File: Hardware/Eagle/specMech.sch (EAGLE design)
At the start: 88 parts, among them J1 PINHD-1X8-MOLEX-SHROUD, J2 MOLEX-22112022, J3 PINHD-1X8-MOLEX-SHROUD, J4 PINHD-1X8-MOLEX-SHROUD, J6 Molex 0022232081, J7 Lantronix XPORT, J8 Molex 0022232081, U1 MCP23008-E/SO, U10 ADS1115, U11 MCP23008-E/SO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

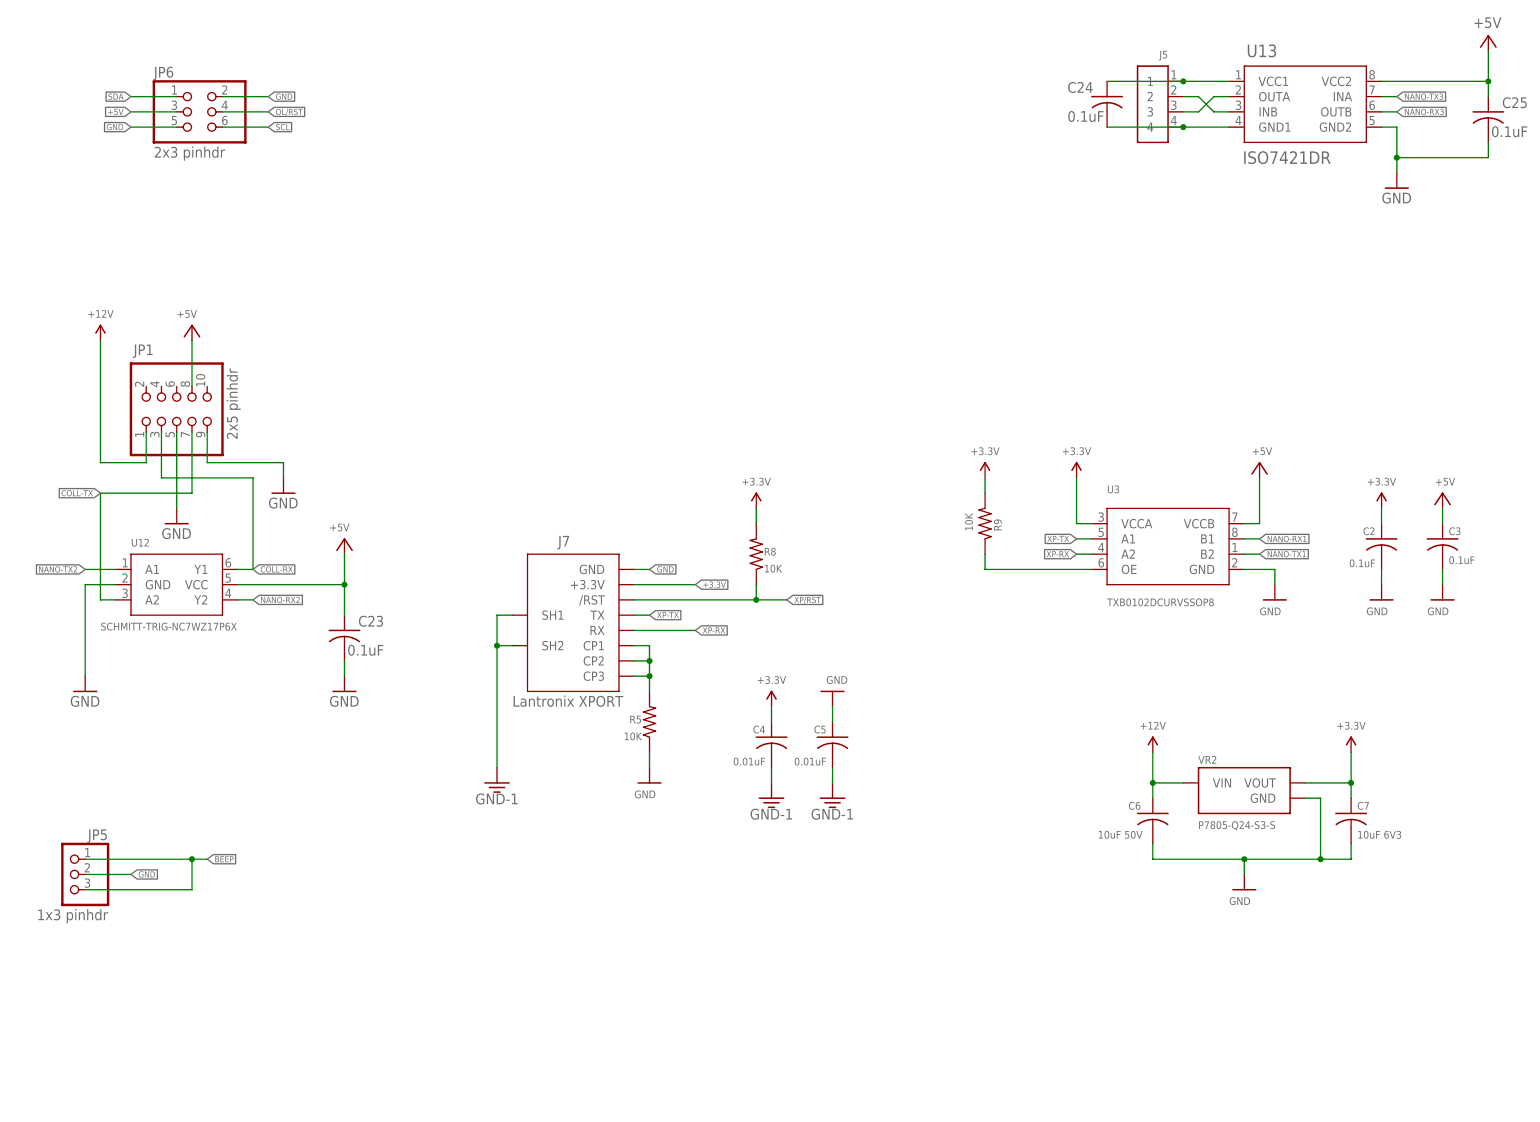
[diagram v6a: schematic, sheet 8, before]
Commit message: Added fan control
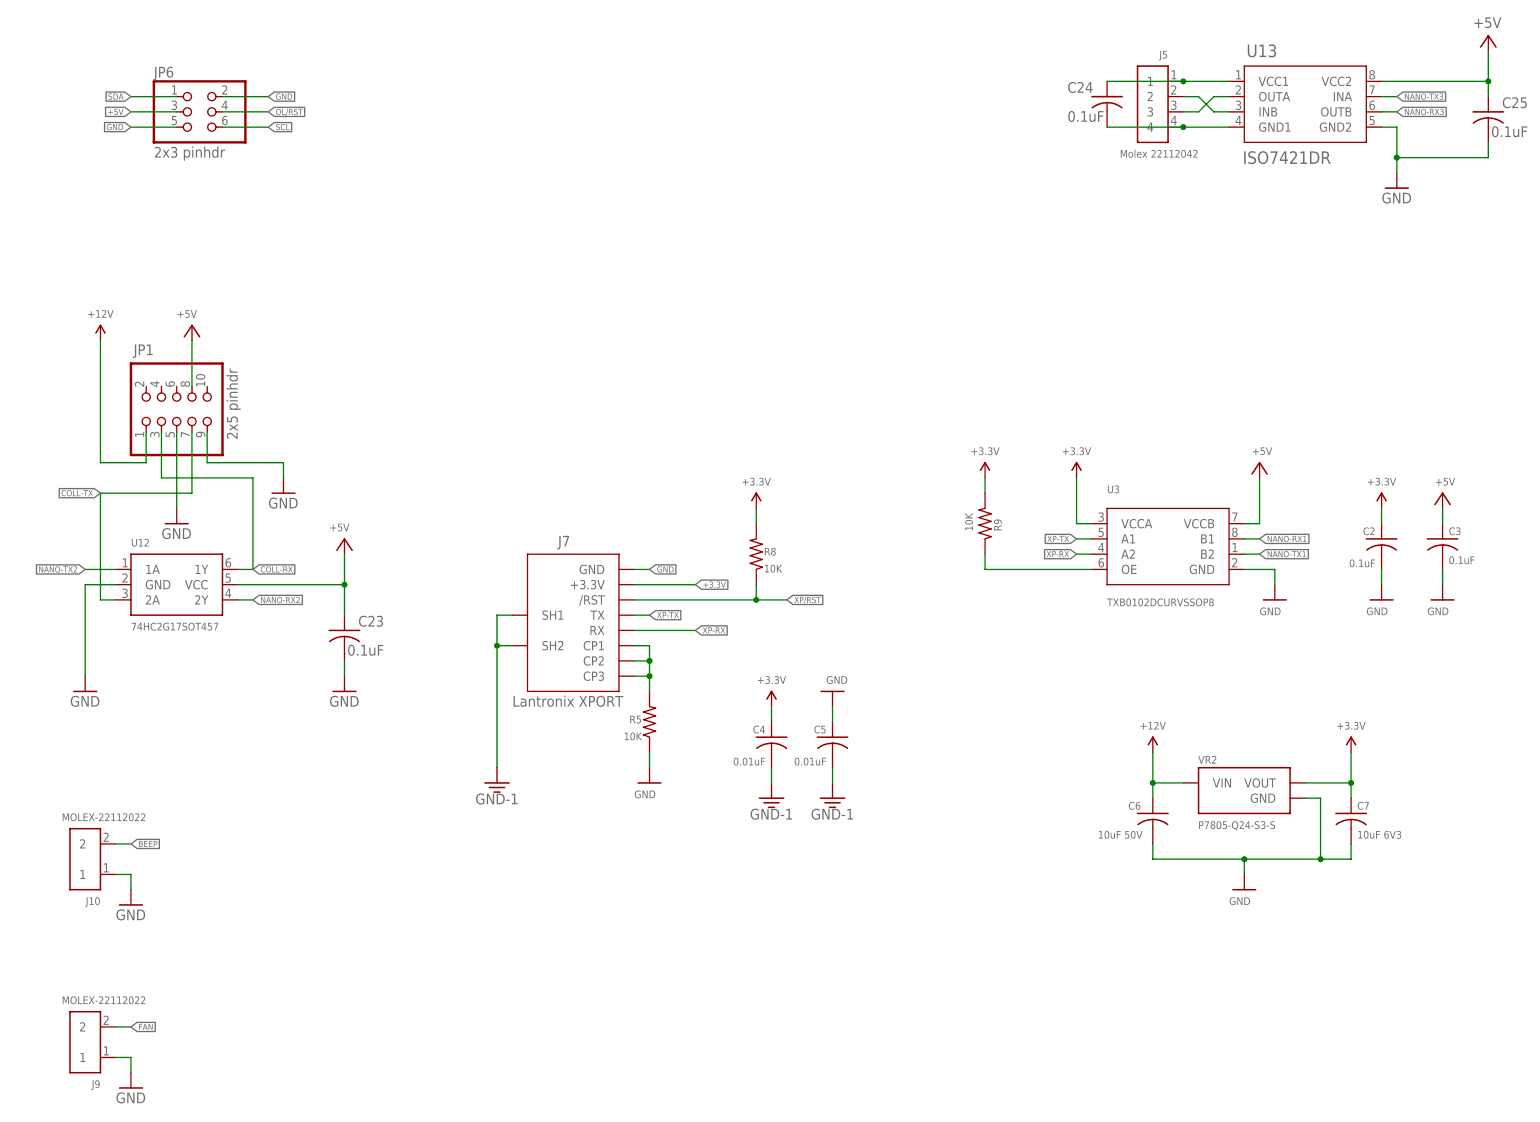
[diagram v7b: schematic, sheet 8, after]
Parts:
- removed JP5: 1x3 pinhdr, AUmlib:PINHD-1X3
- added J10, J9: MOLEX-22112022, AUmlib:PINHD-1X2-MOLEX-22112022
- J5: value (none) -> Molex 22112042
- U12: value SCHMITT-TRIG-NC7WZ17P6X -> 74HC2G17SOT457; device AUmlib:SCHMITT-TRIG-NC7WZ17P6X -> AUmlib:74HC2G17SOT457
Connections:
- new net FAN: CNANO1.PB3, J9.2
- net BEEP: now also J10.2; no longer JP5.1, JP5.3
- net COLL-RX: now also U12.1Y; no longer U12.Y1
- net COLL-TX: now also U12.2A; no longer U12.A2
- net GND: now also J10.1, J9.1; no longer JP5.2
- net NANO-RX2: now also U12.2Y; no longer U12.Y2
- net NANO-TX2: now also U12.1A; no longer U12.A1
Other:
- note added: "Fan"
- note removed: "Change to 2-pin polarized header"
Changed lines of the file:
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@@
 <setting verticaltext="up"/>
 </settings>
-<grid distance="0.1" unitdist="inch" unit="inch" style="lines" multiple="1" display="yes" altdistance="0.01" altunitdist="inch" altunit="inch"/>
+<grid distance="0.1" unitdist="inch" unit="inch" style="lines" multiple="1" display="no" altdistance="0.01" altunitdist="inch" altunit="inch"/>
 <layers>
 <layer number="1" name="Top" color="4" fill="1" visible="no" active="no"/>
@@
 <part name="JP6" library="AUmlib" library_urn="urn:adsk.eagle:library:9166017" deviceset="PINHD-2X3" device="" package3d_urn="urn:adsk.eagle:package:24493429/1" value="2x3 pinhdr"/>
 <part name="JP1" library="AUmlib" library_urn="urn:adsk.eagle:library:9166017" deviceset="PINHD-2X5" device="" package3d_urn="urn:adsk.eagle:package:24435877/1" value="2x5 pinhdr"/>
-<part name="U12" library="AUmlib" library_urn="urn:adsk.eagle:library:9166017" deviceset="SCHMITT-TRIG-NC7WZ17P6X" device="" package3d_urn="urn:adsk.eagle:package:26421290/2"/>
+<part name="U12" library="AUmlib" library_urn="urn:adsk.eagle:library:9166017" deviceset="74HC2G17" device="SOT457" package3d_urn="urn:adsk.eagle:package:9152015/2"/>
 <part name="GND28" library="AUmlib" library_urn="urn:adsk.eagle:library:9166017" deviceset="GND" device=""/>
 <part name="P+12" library="AUmlib" library_urn="urn:adsk.eagle:library:9166017" deviceset="+5V" device=""/>
@@
 <part name="GND41" library="AUmlib" library_urn="urn:adsk.eagle:library:9166017" deviceset="GND" device=""/>
 <part name="GND42" library="AUmlib" library_urn="urn:adsk.eagle:library:9166017" deviceset="GND" device=""/>
-<part name="JP5" library="AUmlib" library_urn="urn:adsk.eagle:library:9166017" deviceset="PINHD-1X3" device="" package3d_urn="urn:adsk.eagle:package:21589412/1" value="1x3 pinhdr"/>
 <part name="U7" library="AUmlib" library_urn="urn:adsk.eagle:library:9166017" deviceset="LTC4311ISC6TRPBF" device="" package3d_urn="urn:adsk.eagle:package:24435366/2"/>
 <part name="C22" library="AUmlib" library_urn="urn:adsk.eagle:library:9166017" deviceset="C-US" device="C0805" package3d_urn="urn:adsk.eagle:package:4021265/3" value="0.1uF"/>
@@
 <part name="TVS1" library="AUmlib" library_urn="urn:adsk.eagle:library:9166017" deviceset="TVS-QUAD-ESDA6V1BC6" device="" package3d_urn="urn:adsk.eagle:package:25920714/2"/>
 <part name="TVS2" library="AUmlib" library_urn="urn:adsk.eagle:library:9166017" deviceset="TVS-QUAD-ESDA6V1BC6" device="" package3d_urn="urn:adsk.eagle:package:25920714/2"/>
-<part name="J5" library="AUmlib" library_urn="urn:adsk.eagle:library:9166017" deviceset="PINHD-1X4-MOLEX-22112042" device="" package3d_urn="urn:adsk.eagle:package:24729143/2"/>
+<part name="J5" library="AUmlib" library_urn="urn:adsk.eagle:library:9166017" deviceset="PINHD-1X4-MOLEX-22112042" device="" package3d_urn="urn:adsk.eagle:package:24729143/2" value="Molex 22112042"/>
+<part name="J9" library="AUmlib" library_urn="urn:adsk.eagle:library:9166017" deviceset="PINHD-1X2-MOLEX-22112022" device="" package3d_urn="urn:adsk.eagle:package:24727026/5" value="MOLEX-22112022"/>
+<part name="GND46" library="AUmlib" library_urn="urn:adsk.eagle:library:9166017" deviceset="GND" device=""/>
+<part name="J10" library="AUmlib" library_urn="urn:adsk.eagle:library:9166017" deviceset="PINHD-1X2-MOLEX-22112022" device="" package3d_urn="urn:adsk.eagle:package:24727026/5" value="MOLEX-22112022"/>
+<part name="GND47" library="AUmlib" library_urn="urn:adsk.eagle:library:9166017" deviceset="GND" device=""/>
 </parts>
 <sheets>
@@
 </segment>
 </net>
+<net name="FAN" class="0">
+<segment>
+<pinref part="CNANO1" gate="G$1" pin="PB3"/>
+<wire x1="88.9" y1="91.44" x2="86.36" y2="91.44" width="0.1524" layer="91"/>
+<label x="86.36" y="91.44" size="1.016" layer="95" rot="R180" xref="yes"/>
+</segment>
+</net>
 </nets>
 </sheet>
@@
 to maintain 3.3 V signaling.</text>
 <text x="190.5" y="167.64" size="1.778" layer="250">Change to 4-pin Molex 22112042 gold pin</text>
-<text x="50.8" y="48.26" size="1.778" layer="250">Change to 2-pin
-polarized header</text>
 <text x="53.34" y="144.78" size="1.778" layer="250">Use old RS-232
 cabling</text>
+<wire x1="12.7" y1="38.1" x2="76.2" y2="38.1" width="0.1524" layer="250"/>
+<wire x1="76.2" y1="38.1" x2="76.2" y2="15.24" width="0.1524" layer="250"/>
+<wire x1="76.2" y1="15.24" x2="12.7" y2="15.24" width="0.1524" layer="250"/>
+<wire x1="12.7" y1="15.24" x2="12.7" y2="38.1" width="0.1524" layer="250"/>
+<text x="68.58" y="33.02" size="2.54" layer="250" ratio="10">Fan</text>
 </plain>
 <instances>
@@
 <instance part="U12" gate="A" x="40.64" y="104.14" smashed="yes">
 <attribute name="NAME" x="33.02" y="110.49" size="1.27" layer="95"/>
-<attribute name="VALUE" x="27.94" y="96.52" size="1.27" layer="96"/>
+<attribute name="VALUE" x="33.02" y="96.52" size="1.27" layer="96"/>
 </instance>
 <instance part="GND28" gate="1" x="25.4" y="86.36" smashed="yes">
@@
 <attribute name="VALUE" x="236.22" y="80.01" size="1.27" layer="96" align="bottom-center"/>
 </instance>
-<instance part="JP5" gate="A" x="22.86" y="55.88" smashed="yes" rot="MR0">
-<attribute name="NAME" x="29.21" y="61.595" size="1.778" layer="95" rot="MR0"/>
-<attribute name="VALUE" x="29.21" y="48.26" size="1.778" layer="96" rot="MR0"/>
-</instance>
 <instance part="J7" gate="G$1" x="106.68" y="96.52" smashed="yes">
 <attribute name="NAME" x="104.14" y="110.49" size="1.778" layer="95"/>
@@
 <instance part="J5" gate="G$1" x="203.2" y="182.88" smashed="yes" rot="MR0">
 <attribute name="NAME" x="205.74" y="191.77" size="1.27" layer="95" rot="MR0"/>
-<attribute name="VALUE" x="205.74" y="175.26" size="1.27" layer="96" rot="MR0"/>
+<attribute name="VALUE" x="210.82" y="175.26" size="1.27" layer="96" rot="MR0"/>
+</instance>
+<instance part="J9" gate="G$1" x="25.4" y="27.94" smashed="yes" rot="R180">
+<attribute name="NAME" x="27.94" y="21.59" size="1.27" layer="95" rot="R180"/>
+<attribute name="VALUE" x="35.56" y="35.56" size="1.27" layer="95" rot="R180"/>
+</instance>
+<instance part="GND46" gate="1" x="33.02" y="20.32" smashed="yes">
+<attribute name="VALUE" x="30.48" y="17.78" size="1.778" layer="96"/>
+</instance>
+<instance part="J10" gate="G$1" x="25.4" y="58.42" smashed="yes" rot="R180">
+<attribute name="NAME" x="27.94" y="52.07" size="1.27" layer="95" rot="R180"/>
+<attribute name="VALUE" x="35.56" y="66.04" size="1.27" layer="95" rot="R180"/>
+</instance>
+<instance part="GND47" gate="1" x="33.02" y="50.8" smashed="yes">
+<attribute name="VALUE" x="30.48" y="48.26" size="1.778" layer="96"/>
 </instance>
 </instances>
@@
 </segment>
 <segment>
-<pinref part="JP5" gate="A" pin="2"/>
-<wire x1="25.4" y1="55.88" x2="33.02" y2="55.88" width="0.1524" layer="91"/>
-<label x="33.02" y="55.88" size="1.016" layer="95" ratio="10" xref="yes"/>
+<pinref part="J9" gate="G$1" pin="1"/>
+<wire x1="30.48" y1="25.4" x2="33.02" y2="25.4" width="0.1524" layer="91"/>
+<pinref part="GND46" gate="1" pin="GND"/>
+<wire x1="33.02" y1="25.4" x2="33.02" y2="22.86" width="0.1524" layer="91"/>
+</segment>
+<segment>
+<pinref part="J10" gate="G$1" pin="1"/>
+<wire x1="30.48" y1="55.88" x2="33.02" y2="55.88" width="0.1524" layer="91"/>
+<pinref part="GND47" gate="1" pin="GND"/>
+<wire x1="33.02" y1="55.88" x2="33.02" y2="53.34" width="0.1524" layer="91"/>
 </segment>
 </net>
@@
 <net name="COLL-TX" class="0">
 <segment>
-<pinref part="U12" gate="A" pin="A2"/>
+<pinref part="U12" gate="A" pin="2A"/>
 <wire x1="30.48" y1="101.6" x2="27.94" y2="101.6" width="0.1524" layer="91"/>
 <wire x1="27.94" y1="101.6" x2="27.94" y2="119.38" width="0.1524" layer="91"/>
@@
 <net name="COLL-RX" class="0">
 <segment>
-<pinref part="U12" gate="A" pin="Y1"/>
+<pinref part="U12" gate="A" pin="1Y"/>
 <wire x1="50.8" y1="106.68" x2="53.34" y2="106.68" width="0.1524" layer="91"/>
 <wire x1="53.34" y1="106.68" x2="53.34" y2="121.92" width="0.1524" layer="91"/>
@@
 <net name="NANO-RX2" class="0">
 <segment>
-<pinref part="U12" gate="A" pin="Y2"/>
+<pinref part="U12" gate="A" pin="2Y"/>
 <wire x1="50.8" y1="101.6" x2="53.34" y2="101.6" width="0.1524" layer="91"/>
 <label x="53.34" y="101.6" size="1.016" layer="95" xref="yes"/>
@@
 <net name="NANO-TX2" class="0">
 <segment>
-<pinref part="U12" gate="A" pin="A1"/>
+<pinref part="U12" gate="A" pin="1A"/>
 <wire x1="30.48" y1="106.68" x2="25.4" y2="106.68" width="0.1524" layer="91"/>
 <label x="25.4" y="106.68" size="1.016" layer="95" rot="R180" xref="yes"/>
@@
 </segment>
 </net>
-<net name="BEEP" class="0">
-<segment>
-<pinref part="JP5" gate="A" pin="1"/>
-<wire x1="25.4" y1="58.42" x2="43.18" y2="58.42" width="0.1524" layer="91"/>
-<label x="45.72" y="58.42" size="1.016" layer="95" ratio="10" xref="yes"/>
-<pinref part="JP5" gate="A" pin="3"/>
-<wire x1="43.18" y1="58.42" x2="45.72" y2="58.42" width="0.1524" layer="91"/>
-<wire x1="25.4" y1="53.34" x2="43.18" y2="53.34" width="0.1524" layer="91"/>
-<wire x1="43.18" y1="53.34" x2="43.18" y2="58.42" width="0.1524" layer="91"/>
-<junction x="43.18" y="58.42"/>
-</segment>
-</net>
 <net name="N$8" class="0">
 <segment>
@@
 </segment>
 </net>
+<net name="FAN" class="0">
+<segment>
+<pinref part="J9" gate="G$1" pin="2"/>
+<wire x1="30.48" y1="30.48" x2="33.02" y2="30.48" width="0.1524" layer="91"/>
+<label x="33.02" y="30.48" size="1.016" layer="95" xref="yes"/>
+</segment>
+</net>
+<net name="BEEP" class="0">
+<segment>
+<pinref part="J10" gate="G$1" pin="2"/>
+<wire x1="30.48" y1="60.96" x2="33.02" y2="60.96" width="0.1524" layer="91"/>
+<label x="33.02" y="60.96" size="1.016" layer="95" xref="yes"/>
+</segment>
+</net>

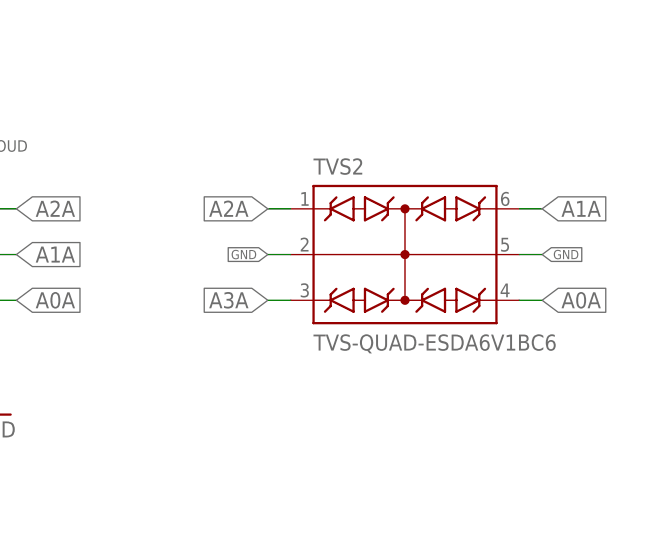
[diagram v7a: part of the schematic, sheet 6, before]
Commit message: Changed to 7-bit TWI addresses everywhere
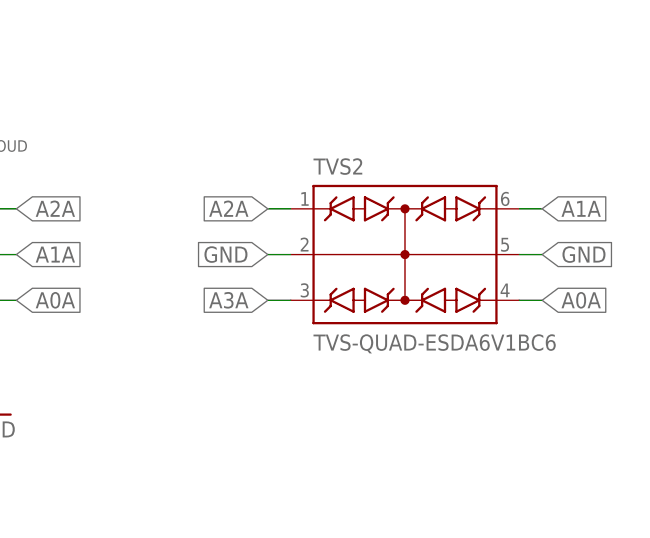
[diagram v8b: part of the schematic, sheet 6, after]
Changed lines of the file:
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@@
 <setting verticaltext="up"/>
 </settings>
-<grid distance="0.1" unitdist="inch" unit="inch" style="lines" multiple="1" display="no" altdistance="0.01" altunitdist="inch" altunit="inch"/>
+<grid distance="0.1" unitdist="inch" unit="inch" style="lines" multiple="1" display="yes" altdistance="0.01" altunitdist="inch" altunit="inch"/>
 <layers>
 <layer number="1" name="Top" color="4" fill="1" visible="no" active="no"/>
@@
 <pinref part="TVS2" gate="G$1" pin="CC1"/>
 <wire x1="226.06" y1="170.18" x2="223.52" y2="170.18" width="0.1524" layer="91"/>
-<label x="223.52" y="170.18" size="1.016" layer="95" rot="R180" xref="yes"/>
+<label x="223.52" y="170.18" size="1.778" layer="95" rot="R180" xref="yes"/>
 </segment>
 <segment>
 <pinref part="TVS2" gate="G$1" pin="CC2"/>
 <wire x1="251.46" y1="170.18" x2="254" y2="170.18" width="0.1524" layer="91"/>
-<label x="254" y="170.18" size="1.016" layer="95" xref="yes"/>
-</segment>
-</net>
+<label x="254" y="170.18" size="1.778" layer="95" xref="yes"/>
+</segment>
+</net>
